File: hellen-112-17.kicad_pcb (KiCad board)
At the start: 4 copper layers, 0 parts

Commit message: #3 #4 #5 #6
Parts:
- added F1: 12H1500D, hellen-one-common:PAD-1206-PAD, F.Cu at (173.7, 85.8)
- added F2: 12H1500D, hellen-one-common:PAD-1206-PAD, F.Cu at (173.7, 88.9)
- added F3: 12H1500D, hellen-one-common:PAD-1206-PAD, F.Cu at (173.7, 92.0)
- added G1: LOGO, rusEFI_Lib:LOGO, B.Cu at (128.0, 140.0)
- added G2: LOGO, rusEFI_Lib:LOGO, F.Cu at (127.5, 140.0)
- added J1: rusefi_2x56_pin_conn, rusefi_2x56_pin_connector:rusefi_2x56_pin_connector, F.Cu at (137.4, 60.3)
- added J2: 6437288-2, Connectors:6437288-2, F.Cu at (91.2, 146.4)
- added J3: 6437288-2, Connectors:6437288-2, F.Cu at (142.7, 117.4)
- added M1: Module:mega_mcu100/0.1, hellen-one-mega-mcu100-0.1:mega-mcu100, F.Cu at (195.5, 86.0)
- added M2: Module-power_12and5V-0.2, hellen-one-power_12and5V-0.2:power_12and5V, F.Cu at (175.2, 127.8)
- added P103: Pad, hellen-one-common:PAD-TH, F.Cu at (141.1, 91.2)
- added P104: Pad, hellen-one-common:PAD-TH, F.Cu at (138.6, 91.2)
- added P105: Pad, hellen-one-common:PAD-TH, F.Cu at (143.7, 91.2)
- added P107: Pad, hellen-one-common:PAD-TH, F.Cu at (113.3, 91.2)
- added P108: Pad, hellen-one-common:PAD-TH, F.Cu at (115.9, 91.2)
- added P119: Pad, hellen-one-common:PAD-TH, F.Cu at (133.5, 91.2)
- added P204: Pad, hellen-one-common:PAD-TH, F.Cu at (96.5, 114.3)
- added P205: Pad, hellen-one-common:PAD-TH, F.Cu at (94.0, 114.3)
- added P206: Pad, hellen-one-common:PAD-TH, F.Cu at (99.0, 114.3)
- added P207: Pad, hellen-one-common:PAD-TH, F.Cu at (101.6, 114.3)
- added P208: Pad, hellen-one-common:PAD-TH, F.Cu at (104.1, 114.3)
- added P334: Pad, hellen-one-common:PAD-TH, F.Cu at (136.0, 91.2)
- added P427: Pad, hellen-one-common:PAD-TH, F.Cu at (75.3, 123.2)
- added Q1: ISL9V3040D3S, Package_TO_SOT_SMD:TO-252-2, F.Cu at (69.4, 88.3)
- added Q2: ISL9V3040D3S, Package_TO_SOT_SMD:TO-252-2, F.Cu at (81.4, 88.3)
- added Q3: ISL9V3040D3S, Package_TO_SOT_SMD:TO-252-2, F.Cu at (69.4, 105.2)
- added Q4: ISL9V3040D3S, Package_TO_SOT_SMD:TO-252-2, F.Cu at (81.4, 105.2)
- added R1: 22, hellen-one-common:R0603, F.Cu at (67.1, 96.4)
- added R10: 100k, hellen-one-common:R0603, F.Cu at (83.8, 113.4)
- added R11: DNP, Resistor_SMD:R_2512_6332Metric, F.Cu at (63.4, 104.6)
- added R12: DNP, Resistor_SMD:R_2512_6332Metric, F.Cu at (87.8, 104.6)
- added R13: Jumper-Pad-Pad, hellen-one-common:PAD-0805-PAD, F.Cu at (167.1, 67.9)
- added R14: Jumper-Pad-Pad, hellen-one-common:PAD-0805-PAD, F.Cu at (167.1, 70.8)
- added R2: 100k, hellen-one-common:R0603, F.Cu at (71.7, 96.4)
- added R3: 22, hellen-one-common:R0603, F.Cu at (79.1, 96.4)
- added R4: 100k, hellen-one-common:R0603, F.Cu at (83.8, 96.4)
- added R5: DNP, Resistor_SMD:R_2512_6332Metric, F.Cu at (63.4, 88.3)
- added R6: DNP, Resistor_SMD:R_2512_6332Metric, F.Cu at (87.8, 88.2)
- added R7: 22, hellen-one-common:R0603, F.Cu at (67.0, 113.4)
- added R8: 100k, hellen-one-common:R0603, F.Cu at (71.6, 113.4)
- added R9: 22, hellen-one-common:R0603, F.Cu at (79.0, 113.4)
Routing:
- net /102_out: track 0.00 -> 162.3 mm
- net /101_out: track 0.00 -> 157.9 mm
- net /ANALOG_SUPPLY_MAP: track 0.00 -> 148.3 mm
- net /THROTTLE_POSITION_2: track 0.00 -> 135.2 mm
- net GND_B50: track 0.00 -> 128.7 mm, vias 0 -> 5
- net /MAP: track 0.00 -> 126.5 mm
- net /CAM: track 0.00 -> 118.8 mm
- net GND: track 0.00 -> 117.6 mm
- net /INJ3: track 0.00 -> 114.3 mm
- net GND_B7: track 0.00 -> 112.8 mm
- net +5VP: track 0.00 -> 108.8 mm
- net /IN_VSS: track 0.00 -> 108.5 mm
- net /INJ1: track 0.00 -> 103.8 mm
- net GND_B6: track 0.00 -> 101.6 mm
- net /SWITCH_A36: track 0.00 -> 99.1 mm
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- added copper zone on B.Cu, net /IGN1
- added copper zone on F.Cu, net /IGN1
- added copper zone on B.Cu, net /IGN2
- added copper zone on F.Cu, net /IGN2
- added copper zone on B.Cu, net /IGN3
- added copper zone on F.Cu, net /IGN3
- added copper zone on B.Cu, net /IGN4
- added copper zone on F.Cu, net /IGN4
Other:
- board outline added: 86.3 x 97.1 mm
- copper layers 4 -> 2
- board text added: "+12V_RELAY"
- board text added: "+5VP"
- board text added: "3V3"
- board text added: "A1"
- board text added: "A10"
- board text added: "A17"
- board text added: "A18"
- board text added: "A2"
- board text added: "A22"
- board text added: "A23"
- board text added: "A24"
- board text added: "A39"
- board text added: "A43"
- board text added: "A45"
- board text added: "A46"
- board text added: "A48"
- board text added: "A49"
- board text added: "A50"
- board text added: "A8"
- board text added: "A9"
- board text added: "B11"
- board text added: "B12"
- board text added: "B2"
- board text added: "B25"
- board text added: "B26"
- board text added: "B28"
- board text added: "B29"
- board text added: "B30"
- board text added: "B34"
- board text added: "B35"
- board text added: "B36"
- board text added: "B39"
- board text added: "B40"
- board text added: "B41"
- board text added: "B48"
- board text added: "B49"
- board text added: "B8"
- board text added: "B9"
- board text added: "CAM"
- board text added: "CAN+"
- board text added: "CAN-"
- board text added: "CASE BOTTOM"
- board text added: "CASE TOP"
- board text added: "CLT"
- board text added: "COIL1"
- board text added: "COIL2"
- board text added: "COIL3"
- board text added: "COIL4"
- board text added: "CRANK_VR+"
- board text added: "CRANK_VR-"
- board text added: "CR_VR+"
- board text added: "Condit"
- board text added: "Conditioner"
- board text added: "ETB+"
- board text added: "ETB-"
- board text added: "FAN"
- board text added: "FUEL_LVL"
- board text added: "GND"
- board text added: "GNDA"
- board text added: "IAT"
- board text added: "IN1"
- board text added: "IN2"
- board text added: "IN3"
- board text added: "IN4"
- board text added: "INJ1"
- board text added: "INJ2"
- board text added: "INJ3"
- board text added: "INJ4"
- board text added: "IN_ANALOG"
- board text added: "IN_BRAKE"
- board text added: "K-LINE"
- board text added: "KEY"
- board text added: "KN1"
- board text added: "KN2"
- board text added: "KNOCK1"
- board text added: "KNOCK2"
- board text added: "Kline"
- board text added: "MAF"
- board text added: "MAP"
- board text added: "OUT_LS"
- board text added: "OUT_RELAY_A51"
- board text added: "OUT_RELAY_A52"
- board text added: "OUT_TACH"
- board text added: "O_FUEL"
- board text added: "O_TACH"
- board text added: "PP1"
- board text added: "PP2"
- board text added: "PRESSURE"
- board text added: "PUMP"
- board text added: "REL"
- board text added: "RELAY"
- board text added: "R_CNTRL"
- board text added: "SW"
- board text added: "SWCH"
- board text added: "SWITCH_A34"
- board text added: "SWITCH_A35"
- board text added: "SW_A36"
- board text added: "S_MAP"
- board text added: "THR_POS_1"
- board text added: "TP2"
- board text added: "TPS"
- board text added: "VVS"
- board text added: "adapter-board-me17-112 rev.B"
- board text added: "locked"

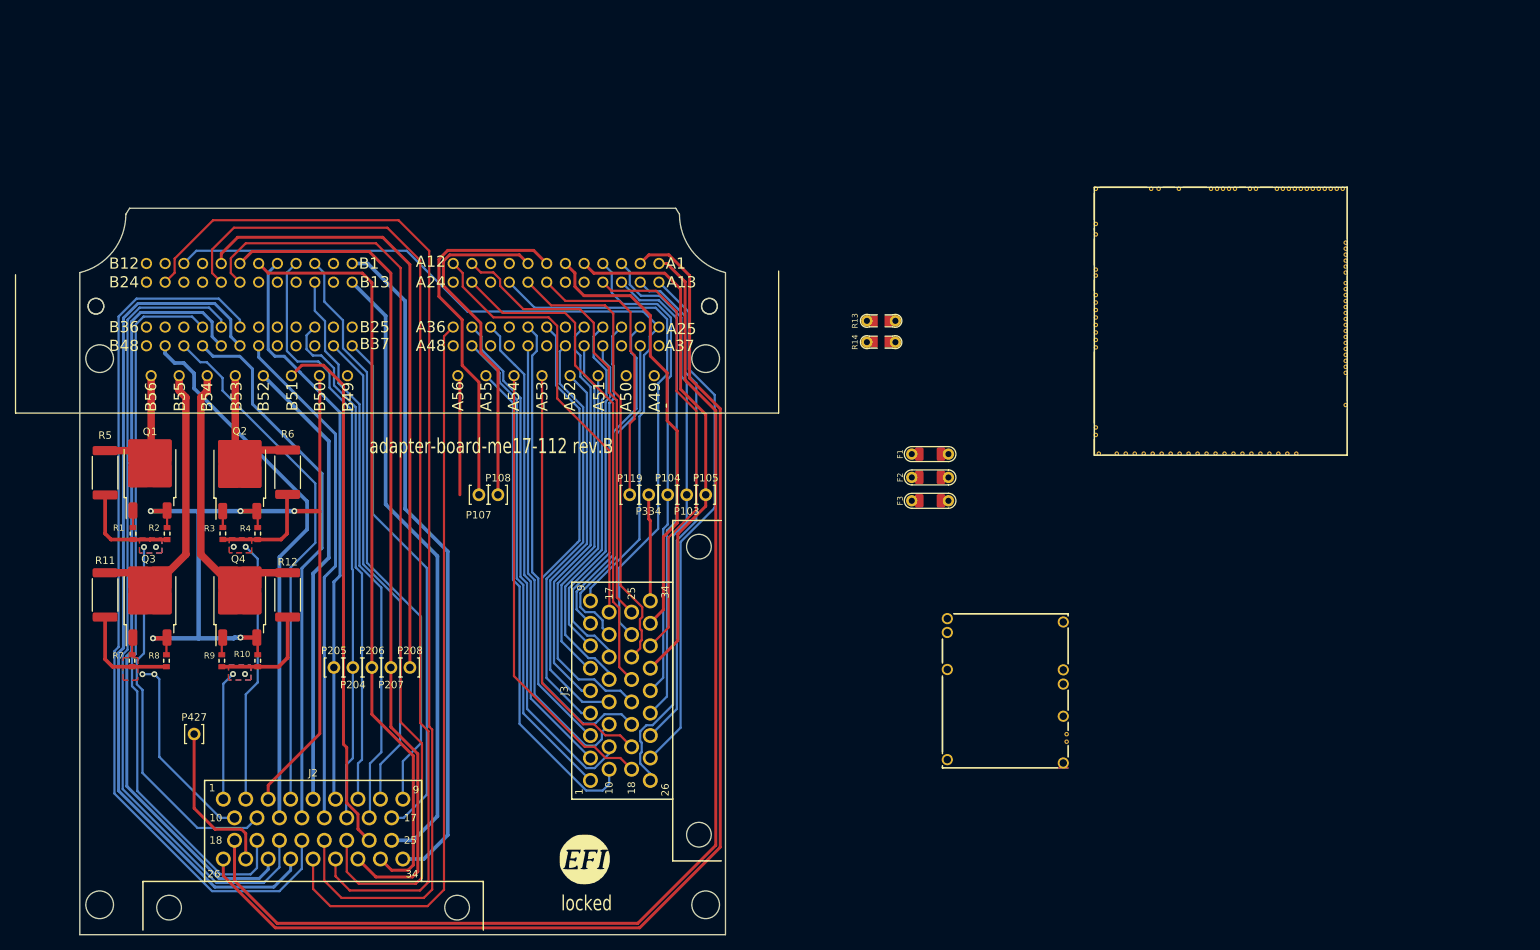
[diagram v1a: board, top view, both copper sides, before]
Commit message: пронумеровала, перенесла изменения на плату
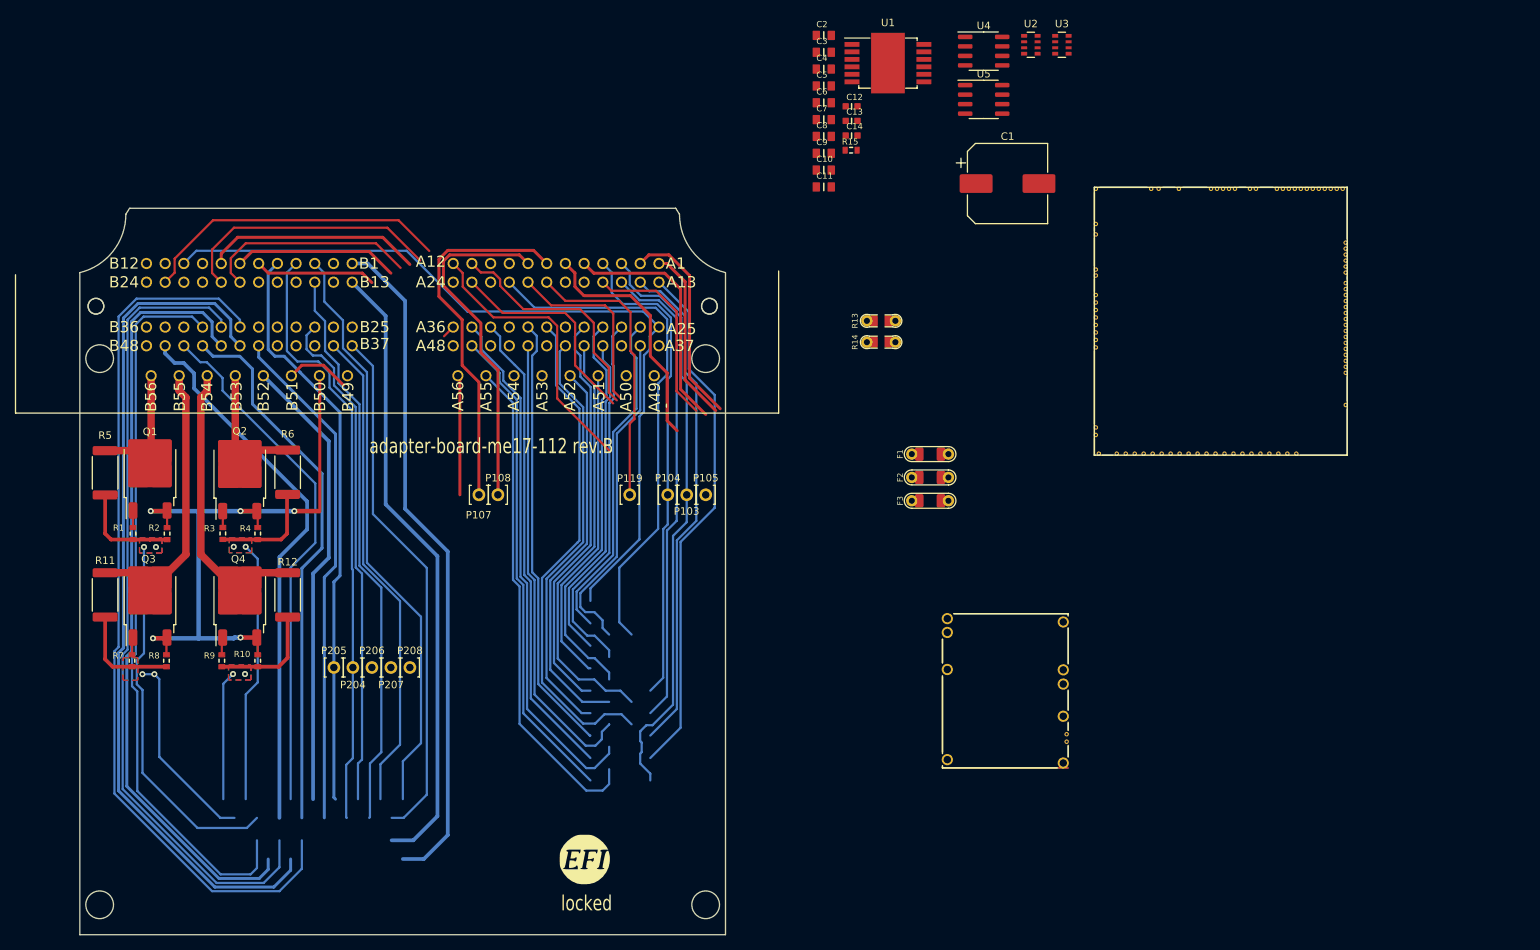
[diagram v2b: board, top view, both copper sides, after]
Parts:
- removed J2, J3: 6437288-2, Connectors:6437288-2
- removed P334, P427: Pad, hellen-one-common:PAD-TH
- added C1: 470uF, Capacitor_SMD:CP_Elec_10x10.5, F.Cu at (184.0, 49.6)
- added C10: 10u, hellen-one-common:C0805, F.Cu at (159.4, 47.8)
- added C11: 10u, hellen-one-common:C0805, F.Cu at (159.4, 50.0)
- added C12: 100n, hellen-one-common:C0603, F.Cu at (163.2, 39.3)
- added C13: 10n, hellen-one-common:C0603, F.Cu at (163.2, 41.2)
- added C14: 10n, hellen-one-common:C0603, F.Cu at (163.2, 43.2)
- added C2: 10u, hellen-one-common:C0805, F.Cu at (159.4, 29.8)
- added C3: 10u, hellen-one-common:C0805, F.Cu at (159.4, 32.0)
- added C4: 10u, hellen-one-common:C0805, F.Cu at (159.4, 34.3)
- added C5: 10u, hellen-one-common:C0805, F.Cu at (159.4, 36.5)
- added C6: 10u, hellen-one-common:C0805, F.Cu at (159.4, 38.8)
- added C7: 10u, hellen-one-common:C0805, F.Cu at (159.4, 41.0)
- added C8: 10u, hellen-one-common:C0805, F.Cu at (159.4, 43.3)
- added C9: 10u, hellen-one-common:C0805, F.Cu at (159.4, 45.5)
- added R15: 4.7k, hellen-one-common:R0603, F.Cu at (163.1, 45.1)
- added U1: TLE9201SG, Package_SO:Infineon_PG-DSO-12-11, F.Cu at (168.0, 33.5)
- added U2: 1k, Resistor_SMD:R_Array_Convex_4x0603, F.Cu at (187.1, 31.1)
- added U3: 1k, Resistor_SMD:R_Array_Convex_4x0603, F.Cu at (191.3, 31.1)
- added U4: VNLD5160, Package_SO:SOIC-8_3.9x4.9mm_P1.27mm, F.Cu at (180.8, 31.9)
- added U5: VNLD5160, Package_SO:SOIC-8_3.9x4.9mm_P1.27mm, F.Cu at (180.8, 38.4)
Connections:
- M1 pad E14: unconnected-(M1-OUT_INJ4_(PD10)-PadE14) -> /lowside_quad/IN4
- M1 pad E15: unconnected-(M1-OUT_INJ3_(PD11)-PadE15) -> /lowside_quad/IN2
- M1 pad E16: unconnected-(M1-OUT_INJ2_(PA9)-PadE16) -> /lowside_quad/IN3
- M1 pad E17: unconnected-(M1-OUT_INJ1_(PD3)-PadE17) -> /lowside_quad/IN1
- M1 pad E18: unconnected-(M1-OUT_PWM1_(PD13)-PadE18) -> /ETB_PWM
- M1 pad E5: /IN_VIGN -> /VIGN
- M1 pad N17: unconnected-(M1-VBAT-PadN17) -> /VBAT
- M1 pad W10: /COIL1 output -> /IGN1
- M1 pad W7: /COIL4 output -> /IGN4
- M1 pad W8: /COIL3 output -> /IGN3
- M1 pad W9: /COIL2 output -> /IGN2
- M2 pad E1: unconnected-(M2-VBAT-PadE1) -> /VBAT
- M2 pad V4: +5VA -> +5VP
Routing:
- net /102_out: track 162.3 -> 27.7 mm
- net /101_out: track 157.9 -> 23.4 mm
- net GND: track 117.6 -> 0.00 mm
- net /ANALOG_SUPPLY_MAP: track 148.3 -> 41.5 mm
- net /THROTTLE_POSITION_2: track 135.2 -> 35.7 mm
- net /MAP: track 126.5 -> 28.6 mm
- net /SWITCH_A36: track 99.1 -> 1.74 mm
- net GND_B7: track 112.8 -> 22.0 mm
- net GND_B6: track 101.6 -> 16.2 mm
- net /ETB+: track 70.9 -> 0.00 mm
- net Net-(F1-Pad1): track 0.00 -> 66.4 mm
- net (no net): track 66.4 -> 0.00 mm
- net Net-(J1-PadB52): track 0.00 -> 61.1 mm
- net /ETB-: track 61.1 -> 0.00 mm
- net /VOLTAGE_FROM_KEY: track 59.8 -> 0.00 mm
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
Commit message: Upd SCH
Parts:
- removed P103, P104, P105, P107, P108, P119, P204, P205, P206, P207, P208: Pad, hellen-one-common:PAD-TH
- removed U2, U3: 1k, Resistor_SMD:R_Array_Convex_4x0603
- added D1: PSM712-LF, hellen-one-common:SOT-23, F.Cu at (121.0, 98.6)
- added D2: B5819W, hellen-one-common:SOD-123, F.Cu at (134.5, 105.0)
- added D3: B5819W, hellen-one-common:SOD-123, F.Cu at (128.5, 110.5)
- added D4: B5819W, hellen-one-common:SOD-123, F.Cu at (134.5, 110.5)
- added D5: B5819W, hellen-one-common:SOD-123, F.Cu at (116.5, 105.0)
- added D6: B5819W, hellen-one-common:SOD-123, F.Cu at (122.5, 105.0)
- added D7: B5819W, hellen-one-common:SOD-123, F.Cu at (128.5, 105.0)
- added D8: B5819W, hellen-one-common:SOD-123, F.Cu at (128.5, 116.0)
- added D9: B5819W, hellen-one-common:SOD-123, F.Cu at (134.5, 116.0)
- added J2: USB_B_Mini, hellen-one-common:USB-MINI-B-VERTICAL, F.Cu at (81.6, 113.7)
- added M3: Module-knock-0.2, hellen-one-knock-0.2:knock, F.Cu at (93.5, 88.0)
- added M4: Module:mega_mcu100/0.1, hellen-one-mega-mcu100-0.1:mega-mcu100, F.Cu at (121.9, 145.0)
- added M5: Module-lin-0.1, hellen-one-lin-0.1:lin, F.Cu at (116.9, 88.8)
- added Q10: AO3400A, hellen-one-common:SOT-23, F.Cu at (125.5, 104.5)
- added Q11: AO3400A, hellen-one-common:SOT-23, F.Cu at (131.5, 104.5)
- added Q12: AO3400A, hellen-one-common:SOT-23, F.Cu at (131.5, 115.5)
- added Q13: AO3400A, hellen-one-common:SOT-23, F.Cu at (137.5, 115.5)
- added Q5: AO3400A, hellen-one-common:SOT-23, F.Cu at (137.5, 104.5)
- added Q6: AO3400A, hellen-one-common:SOT-23, F.Cu at (131.5, 110.0)
- added Q7: AO3400A, hellen-one-common:SOT-23, F.Cu at (137.5, 110.0)
- added Q8: AO3400A, hellen-one-common:SOT-23, F.Cu at (117.5, 98.6)
- added Q9: AO3400A, hellen-one-common:SOT-23, F.Cu at (119.5, 104.4)
- added R16: Jumper-Pad-Pad, hellen-one-common:PAD-0805-PAD, F.Cu at (84.5, 84.5)
- added R17: 4.7k, hellen-one-common:R0603, F.Cu at (84.0, 129.5)
- added R18: 4.7k, hellen-one-common:R0603, F.Cu at (82.5, 88.5)
- added R19: 4.7k, Resistor_SMD:R_0603_1608Metric_Pad0.98x0.95mm_HandSolder, F.Cu at (80.5, 131.1)
- added R20: 4.7k, Resistor_SMD:R_0603_1608Metric_Pad0.98x0.95mm_HandSolder, F.Cu at (78.5, 131.1)
- added R33: 4.7k, hellen-one-common:R0603, F.Cu at (137.5, 107.0)
- added R34: 4.7k, hellen-one-common:R0603, F.Cu at (131.5, 112.5)
- added R35: 4.7k, hellen-one-common:R0603, F.Cu at (137.5, 112.5)
- added R36: 4.7k, hellen-one-common:R0603, F.Cu at (117.5, 101.1)
- added R37: 4.7k, hellen-one-common:R0603, F.Cu at (119.5, 107.0)
- added R38: 4.7k, hellen-one-common:R0603, F.Cu at (125.5, 107.0)
- added R39: 4.7k, hellen-one-common:R0603, F.Cu at (131.5, 107.0)
- added R40: 4.7k, hellen-one-common:R0603, F.Cu at (131.5, 118.0)
- added R41: 4.7k, hellen-one-common:R0603, F.Cu at (137.5, 118.0)
- added R44: 1k, Resistor_SMD:R_Array_Convex_4x0603, F.Cu at (125.5, 121.9)
- added R45: 1k, Resistor_SMD:R_Array_Convex_4x0603, F.Cu at (129.1, 121.9)
- added R46: 1k, Resistor_SMD:R_Array_Convex_4x0603, F.Cu at (125.0, 98.0)
- added R47: 1k, Resistor_SMD:R_Array_Convex_4x0603, F.Cu at (129.0, 98.0)
- added U10: VNLD5160, Package_SO:SOIC-8_3.9x4.9mm_P1.27mm, F.Cu at (135.0, 92.5)
- added U11: VNLD5160, Package_SO:SOIC-8_3.9x4.9mm_P1.27mm, F.Cu at (135.0, 99.5)
- added U6: SRV05-4, Package_TO_SOT_SMD:SOT-23-6, F.Cu at (79.5, 135.0)
- added U7: 74VHC163FT, Package_SO:TSSOP-16_4.4x5mm_P0.65mm, F.Cu at (73.0, 133.5)
- C1: value 470uF -> 10u; footprint Capacitor_SMD:CP_Elec_10x10.5 -> hellen-one-common:C0805
- C11: value 10u -> 100n; footprint hellen-one-common:C0805 -> hellen-one-common:C0603
- C12: value 100n -> 10n
- C14: value 10n -> 100n; footprint hellen-one-common:C0603 -> Capacitor_SMD:C_0603_1608Metric_Pad1.08x0.95mm_HandSolder
- G1: value LOGO -> PROTO_AREA; footprint rusEFI_Lib:LOGO -> hellen-one-common:PROTO_AREA; moved to F.Cu
- G2: value LOGO -> PROTO_AREA; footprint rusEFI_Lib:LOGO -> hellen-one-common:PROTO_AREA
- J1: footprint rusefi_2x56_pin_connector:rusefi_2x56_pin_connector -> kicad6-libraries:rusefi_2x56_pin_connector
- M1: value Module:mega_mcu100/0.1 -> Module-power_12and5V-0.2; footprint hellen-one-mega-mcu100-0.1:mega-mcu100 -> hellen-one-power_12and5V-0.2:power_12and5V
- M2: value Module-power_12and5V-0.2 -> Module-vr-max9924-0.1; footprint hellen-one-power_12and5V-0.2:power_12and5V -> hellen-one-vr-max9924-0.1:vr-max9924
- R1, R3, R7, R9: value 22 -> Jumper-Pad-Pad; footprint hellen-one-common:R0603 -> hellen-one-common:PAD-0805-PAD
- R10, R2, R4, R8: value 100k -> Jumper-Pad-Pad; footprint hellen-one-common:R0603 -> hellen-one-common:PAD-0805-PAD
- R11, R12, R5, R6: value DNP -> Jumper-Pad-Pad; footprint Resistor_SMD:R_2512_6332Metric -> hellen-one-common:PAD-0805-PAD
- R15: value 4.7k -> Jumper-Pad-Pad; footprint hellen-one-common:R0603 -> hellen-one-common:PAD-0805-PAD
- moved C14 131.5 mm to (68.0, 134.0), turned to -90 degrees
- moved C1 122.0 mm to (71.6, 97.0), turned to 90 degrees
- moved C12 109.3 mm to (68.0, 93.0), turned to 90 degrees
- moved C2 109.0 mm to (73.6, 97.0), turned to 90 degrees
- moved U1 108.8 mm to (75.4, 90.5)
- moved C3 106.1 mm to (75.6, 97.0), turned to 90 degrees
- moved C4 103.1 mm to (77.6, 97.0), turned to 90 degrees
- moved M1 101.1 mm to (94.4, 88.7), turned to -90 degrees
- moved U4 100.6 mm to (135.0, 121.5)
- moved U5 100.2 mm to (135.0, 127.5)
- moved C5 100.2 mm to (79.6, 97.0), turned to 90 degrees
- moved C11 99.8 mm to (68.0, 90.0), turned to -90 degrees
- moved C6 99.3 mm to (71.1, 84.0), turned to -90 degrees
- moved M2 97.2 mm to (84.2, 93.5), turned to -90 degrees
- moved C7 96.5 mm to (73.1, 84.0), turned to -90 degrees
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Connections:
- C1 pad 1: +12V_ETB -> GND
- C1 pad 2: GND_B50 -> +12V_RAW
- C10 pad 2: +12V_ETB -> +12V_RAW
- C11 pad 2: +12V_ETB -> +12V_RAW
- C12 pad 2: +12V_ETB -> /OUT_ETB-
- C13 pad 2: /ETB- -> /OUT_ETB+
- C14 pad 2: /ETB+ -> +5VA
- C2 pad 2: +12V_ETB -> +12V_RAW
- C3 pad 2: +12V_ETB -> +12V_RAW
- C4 pad 2: +12V_ETB -> +12V_RAW
- C5 pad 2: +12V_ETB -> +12V_RAW
- C6 pad 2: +12V_ETB -> +12V_RAW
- C7 pad 2: +12V_ETB -> +12V_RAW
- C8 pad 2: +12V_ETB -> +12V_RAW
- C9 pad 2: +12V_ETB -> +12V_RAW
- F1 pad 2: +12VA -> /IN_VIGN
- F2 pad 2: +12VA -> +12V_RAW
- F3 pad 2: /VOLTAGE_FROM_KEY -> +12V_RAW
- M1 pad E1: unconnected-(M1-V5A_SWITCHABLE-PadE1) -> /VBAT
- M1 pad E2: unconnected-(M1-GNDA-PadE2) -> +12V
- M1 pad E3: unconnected-(M1-I2C_SCL_(PB10)-PadE3) -> /VIGN
- M1 pad E4: unconnected-(M1-I2C_SDA_(PB11)-PadE4) -> +5V
- M1 pad E5: /VIGN -> /PWR_EN
- M1 pad E6: unconnected-(M1-SPI2_CS_/_CAN2_RX_(PB12)-PadE6) -> /TLS115_PG
- M1 pad S1: unconnected-(M1-IN_D4_(PE15)-PadS1) -> GND
- M2 pad E1: /VBAT -> unconnected-(M2-NC-PadE1)
- M2 pad E2: +12V -> unconnected-(M2-NC-PadE2)
- M2 pad E3: /VIGN -> /CRANK_VR
- M2 pad E4: +5V -> +5VA
- Q1 pad 1: Net-(Q1-G) -> /IGN1
- Q1 pad 2: /COIL1 output -> /OUT_IGN1
- Q1 pad 3: GND_B50 -> GND
- Q2 pad 1: Net-(Q2-G) -> /IGN2
- Q2 pad 2: /COIL2 output -> /OUT_IGN2
- Q2 pad 3: GND_B50 -> GND
- Q3 pad 1: Net-(Q3-G) -> /IGN3
- Q3 pad 2: /COIL4 output -> /OUT_IGN3
- Q3 pad 3: GND_B50 -> GND
- Q4 pad 1: Net-(Q4-G) -> /IGN4
- Q4 pad 2: /COIL3 output -> /OUT_IGN4
- Q4 pad 3: GND_B50 -> GND
- R1 pad 1: Net-(Q1-G) -> Net-(J1-Pad7)
- R1 pad 2: /IGN1 -> /IN_AV_107
- R10 pad 1: GND_B50 -> Net-(J1-Pad69)
- R10 pad 2: /IGN4 -> /IN_CRANK_VR+
- R11 pad 1: /IGN3 -> Net-(J1-Pad79)
- R11 pad 2: /COIL4 output -> +5VP
- R12 pad 1: /IGN4 -> Net-(J1-Pad89)
- R12 pad 2: /COIL3 output -> /IN_MAF_DIGITAL
- R13 pad 1: Net-(J1-PadB51) -> Net-(J1-Pad93)
- R13 pad 2: /ETB+ -> /IN_KNOCK_RAW
- R14 pad 1: Net-(J1-PadB52) -> Net-(J1-Pad94)
- R14 pad 2: /ETB- -> GNDA
- R15 pad 1: /ETB_DIS -> Net-(J1-Pad107)
- R15 pad 2: +3.3V -> /OUT_ETB+
- R2 pad 1: GND_B50 -> Net-(J1-Pad8)
- R2 pad 2: /IGN1 -> GND
- R3 pad 1: Net-(Q2-G) -> Net-(J1-Pad11)
- R3 pad 2: /IGN2 -> /IN_AV_111
- R4 pad 1: GND_B50 -> Net-(J1-Pad14)
- R4 pad 2: /IGN2 -> /IN_PPS2
- R5 pad 1: /IGN1 -> Net-(J1-Pad21)
- R5 pad 2: /COIL1 output -> /IN_PPS1
- R6 pad 1: /IGN2 -> Net-(J1-Pad25)
- R6 pad 2: /COIL2 output -> +5VP
- R7 pad 1: Net-(Q3-G) -> Net-(J1-Pad26)
- R7 pad 2: /IGN3 -> +5VP
- R8 pad 1: GND_B50 -> Net-(J1-Pad38)
- R8 pad 2: /IGN3 -> +5VP
- R9 pad 1: Net-(Q4-G) -> Net-(J1-Pad57)
- R9 pad 2: /IGN4 -> /IN_CRANK_VR-
- U1 pad 4: +12V_ETB -> +12V_RAW
- U1 pad 5: /ETB- -> /OUT_ETB-
- U1 pad 7: /ETB+ -> /OUT_ETB+
- U4 pad 6: /INJ2 -> /OUT_INJ2
- U4 pad 8: /INJ1 -> /OUT_INJ1
- U5 pad 6: /INJ4 -> /OUT_INJ4
- U5 pad 8: /INJ3 -> /OUT_INJ3
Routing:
- net /CAM: track 118.8 -> 0.00 mm
- net /INJ3: track 114.3 -> 0.00 mm
- net +5VP: track 108.8 -> 0.00 mm
- net /IN_VSS: track 108.5 -> 0.00 mm
- net /INJ1: track 103.8 -> 0.00 mm
- net /ANALOG_MAF: track 97.5 -> 0.00 mm
- net /CRANK_VR-: track 90.2 -> 0.00 mm
- net GND_B50: track 87.4 -> 0.00 mm, vias 5 -> 0
- net /CRANK_VR+: track 83.6 -> 0.00 mm
- net GND_B4: track 80.3 -> 0.00 mm
- net /THROTTLE_POSITION_1: track 78.5 -> 0.00 mm
- net GNDA_A3: track 78.0 -> 0.00 mm
- net GND_B5: track 77.2 -> 0.00 mm
- net /CLT: track 76.0 -> 0.00 mm
- net GND_B47: track 73.2 -> 0.00 mm
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- removed copper zone on B.Cu, net /IGN1
- removed copper zone on F.Cu, net /IGN1
- removed copper zone on B.Cu, net /IGN2
- removed copper zone on F.Cu, net /IGN2
- removed copper zone on B.Cu, net /IGN3
- removed copper zone on F.Cu, net /IGN3
- removed copper zone on B.Cu, net /IGN4
- removed copper zone on F.Cu, net /IGN4
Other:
- board text added: "rusEFI.com"
- board text removed: "locked"
